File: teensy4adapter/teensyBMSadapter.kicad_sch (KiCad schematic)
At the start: 11 parts, among them J1 Conn_01x14_Socket, J2 Conn_01x14_Pin, J3 Conn_01x14_Pin, J4 Conn_01x14_Socket

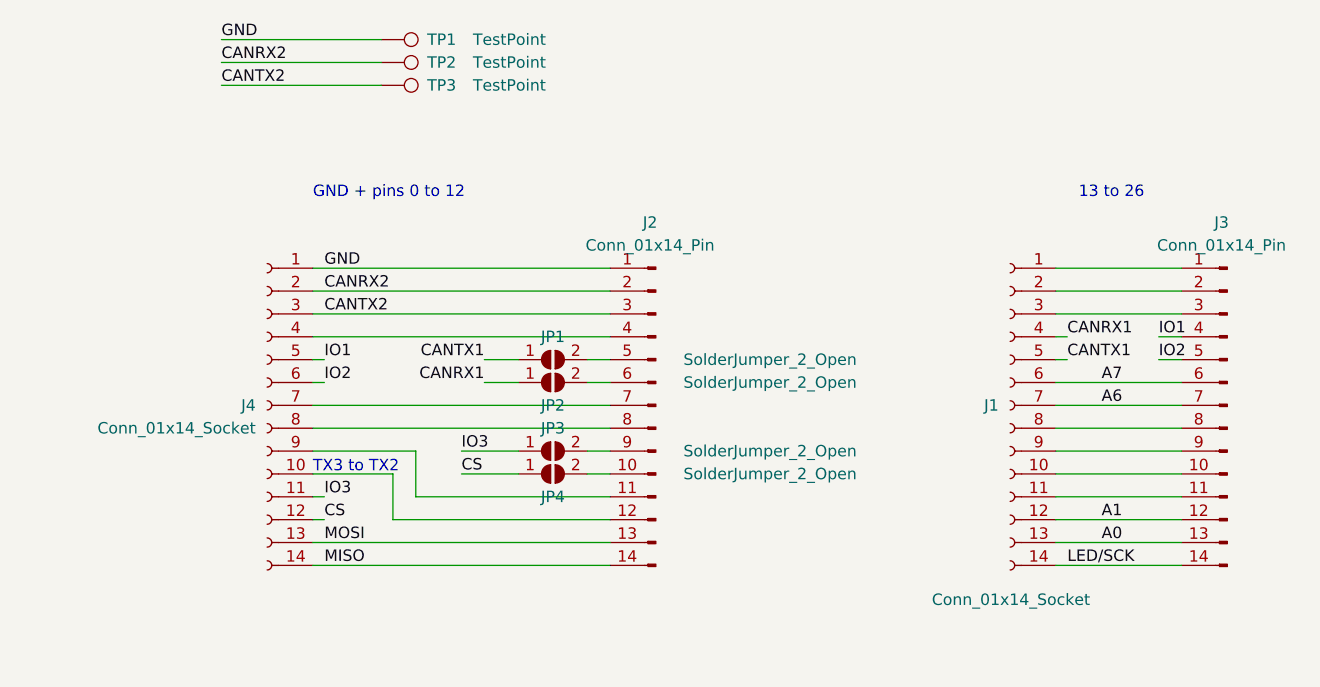
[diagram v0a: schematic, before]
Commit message: kicad: connected UART3 because of the tesla module.
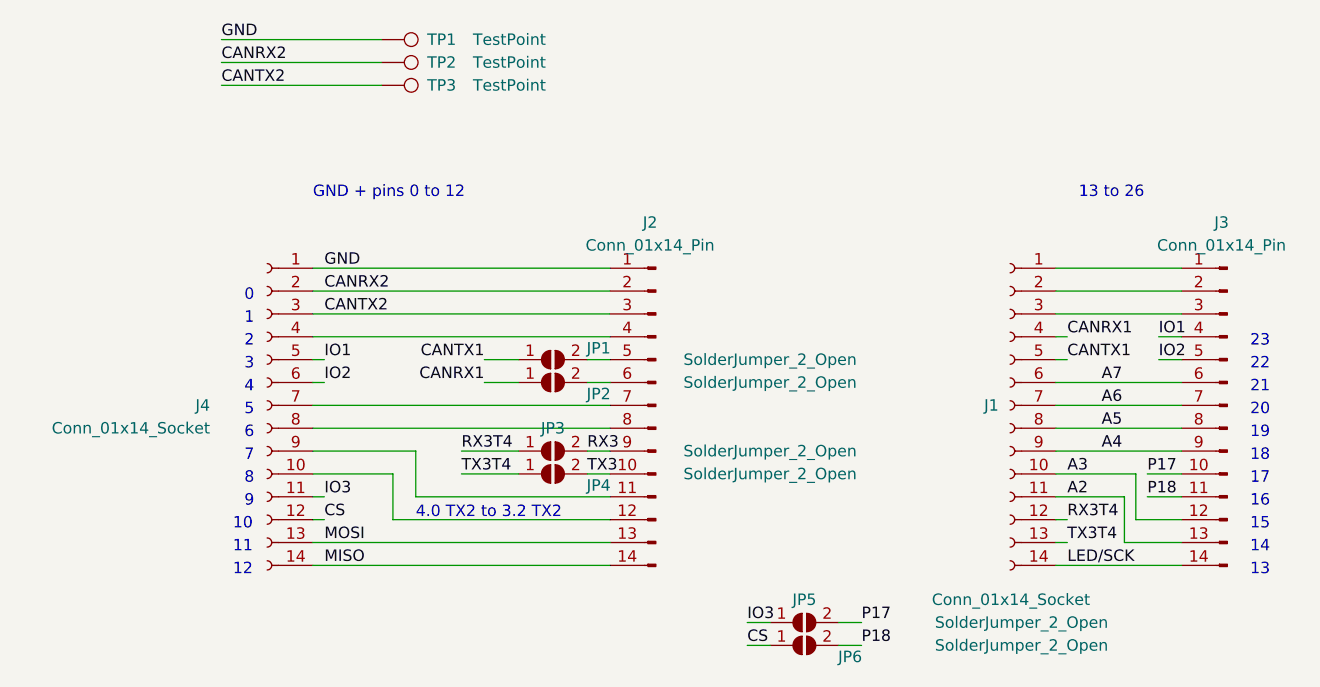
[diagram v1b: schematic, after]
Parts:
- added JP5, JP6: SolderJumper_2_Open, Jumper:SolderJumper-2_P1.3mm_Open_RoundedPad1.0x1.5mm, symbol Jumper:SolderJumper_2_Open
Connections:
- net CS: now also JP6.1 (A); no longer JP4.1 (A)
- net IO3: now also JP5.1 (A); no longer JP3.1 (A)
- net A3: now reaches J1.10 (Pin_10)
- net A3: now also J3.12 (Pin_12); no longer J3.10 (Pin_10)
- net A2: now reaches J1.11 (Pin_11)
- net A2: now also J3.13 (Pin_13); no longer J3.11 (Pin_11)
- net A5: now reaches J1.8 (Pin_8), J3.8 (Pin_8)
- net A4: now reaches J1.9 (Pin_9), J3.9 (Pin_9)
- net RX3: now reaches J2.9 (Pin_9), JP3.2 (B)
- net TX3: now reaches J2.10 (Pin_10), JP4.2 (B)
- net A0 renamed TX3T4
- net TX3T4: now also JP4.1 (A); no longer J3.13 (Pin_13)
- net A1 renamed RX3T4
- net RX3T4: now also JP3.1 (A); no longer J3.12 (Pin_12)
- new net P17: J3.10 (Pin_10), JP5.2 (B)
- new net P18: J3.11 (Pin_11), JP6.2 (B)
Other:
- note added: "0"
- note added: "1"
- note added: "10"
- note added: "11"
- note added: "12"
- note added: "13"
- note added: "14"
- note added: "15"
- note added: "16"
- note added: "17"
- note added: "18"
- note added: "19"
- note added: "2"
- note added: "20"
- note added: "21"
- note added: "22"
- note added: "23"
- note added: "3"
- note added: "4"
- note added: "4.0 TX2 to 3.2 TX2"
- note added: "5"
- note added: "6"
- note added: "7"
- note added: "8"
- note added: "9"
- note removed: "TX3 to TX2"

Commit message: Adding closed solder jumpers to the CAN bus pins
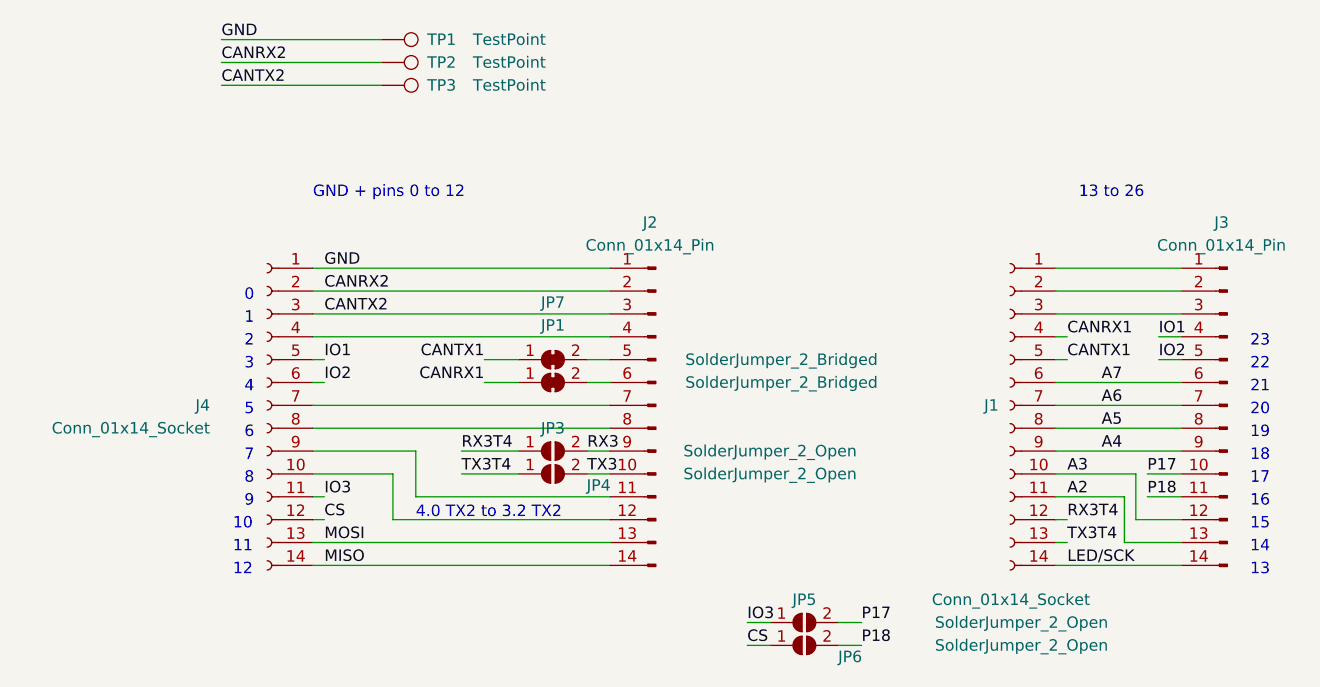
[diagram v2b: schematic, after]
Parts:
- removed JP1, JP2: SolderJumper_2_Open, Jumper:SolderJumper-2_P1.3mm_Open_RoundedPad1.0x1.5mm, symbol Jumper:SolderJumper_2_Open
- added JP1, JP7: SolderJumper_2_Bridged, Jumper:SolderJumper-2_P1.3mm_Bridged_RoundedPad1.0x1.5mm, symbol Jumper:SolderJumper_2_Bridged
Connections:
- net CANRX1: now also JP1.1 (A)
- net CANTX1: now also JP7.1 (A)
- net at J2.6 (Pin_6): now also JP1.2 (B)
- net at J2.5 (Pin_5): now also JP7.2 (B)
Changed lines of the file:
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@@
-    )
-  )
-  (symbol (lib_id "Jumper:SolderJumper_2_Open") (at 121.92 81.28 0) (unit 1)
-    (in_bom yes) (on_board yes) (dnp no)
-    (property "Reference" "JP2" (at 127 82.55 0)
-      (effects (font (size 1.27 1.27)))
-    )
-    (property "Value" "SolderJumper_2_Open" (at 146.05 81.28 0)
-      (effects (font (size 1.27 1.27)))
-    )
-    (property "Footprint" "Jumper:SolderJumper-2_P1.3mm_Open_RoundedPad1.0x1.5mm" (at 121.92 81.28 0)
-      (effects (font (size 1.27 1.27)) hide)
-    )
-    (property "Datasheet" "~" (at 121.92 81.28 0)
-      (effects (font (size 1.27 1.27)) hide)
-    )
-    (pin "1")
-    (pin "2")
-    (instances
-      (project "teensyBMSadapter"
-        (path "/a15f0488-2f03-4fa0-a88c-aed6c7b384e8"
-          (reference "JP2") (unit 1)
-        )
-      )
     )
   )
@@
     )
   )
-  (symbol (lib_id "Jumper:SolderJumper_2_Open") (at 121.92 78.74 0) (unit 1)
-    (in_bom yes) (on_board yes) (dnp no)
-    (property "Reference" "JP1" (at 127 77.47 0)
-      (effects (font (size 1.27 1.27)))
-    )
-    (property "Value" "SolderJumper_2_Open" (at 146.05 78.74 0)
-      (effects (font (size 1.27 1.27)))
-    )
-    (property "Footprint" "Jumper:SolderJumper-2_P1.3mm_Open_RoundedPad1.0x1.5mm" (at 121.92 78.74 0)
+  (symbol (lib_id "Jumper:SolderJumper_2_Bridged") (at 121.92 78.74 0) (unit 1)
+    (in_bom yes) (on_board yes) (dnp no)
+    (property "Reference" "JP7" (at 121.92 72.39 0)
+      (effects (font (size 1.27 1.27)))
+    )
+    (property "Value" "SolderJumper_2_Bridged" (at 147.32 78.74 0)
+      (effects (font (size 1.27 1.27)))
+    )
+    (property "Footprint" "Jumper:SolderJumper-2_P1.3mm_Bridged_RoundedPad1.0x1.5mm" (at 121.92 78.74 0)
       (effects (font (size 1.27 1.27)) hide)
     )
@@
       (project "teensyBMSadapter"
         (path "/a15f0488-2f03-4fa0-a88c-aed6c7b384e8"
-          (reference "JP1") (unit 1)
+          (reference "JP7") (unit 1)
         )
       )
@@
         )
       )
+    )
+  )
+  (symbol (lib_id "Jumper:SolderJumper_2_Bridged") (at 121.92 81.28 0) (unit 1)
+    (in_bom yes) (on_board yes) (dnp no)
+    (property "Reference" "JP1" (at 121.92 74.93 0)
+      (effects (font (size 1.27 1.27)))
+    )
+    (property "Value" "SolderJumper_2_Bridged" (at 147.32 81.28 0)
+      (effects (font (size 1.27 1.27)))
+    )
+    (property "Footprint" "Jumper:SolderJumper-2_P1.3mm_Bridged_RoundedPad1.0x1.5mm" (at 121.92 81.28 0)
+      (effects (font (size 1.27 1.27)) hide)
+    )
+    (property "Datasheet" "~" (at 121.92 81.28 0)
+      (effects (font (size 1.27 1.27)) hide)
+    )
+    (pin "1")
+    (pin "2")
+    (instances
+      (project "teensyBMSadapter"
+        (path "/a15f0488-2f03-4fa0-a88c-aed6c7b384e8"
+          (reference "JP1") (unit 1)
+        )
+      )
